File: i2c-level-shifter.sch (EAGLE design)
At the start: 11 parts, among them IC1 LP298XS, Q1 MMBF170, Q2 MMBF170

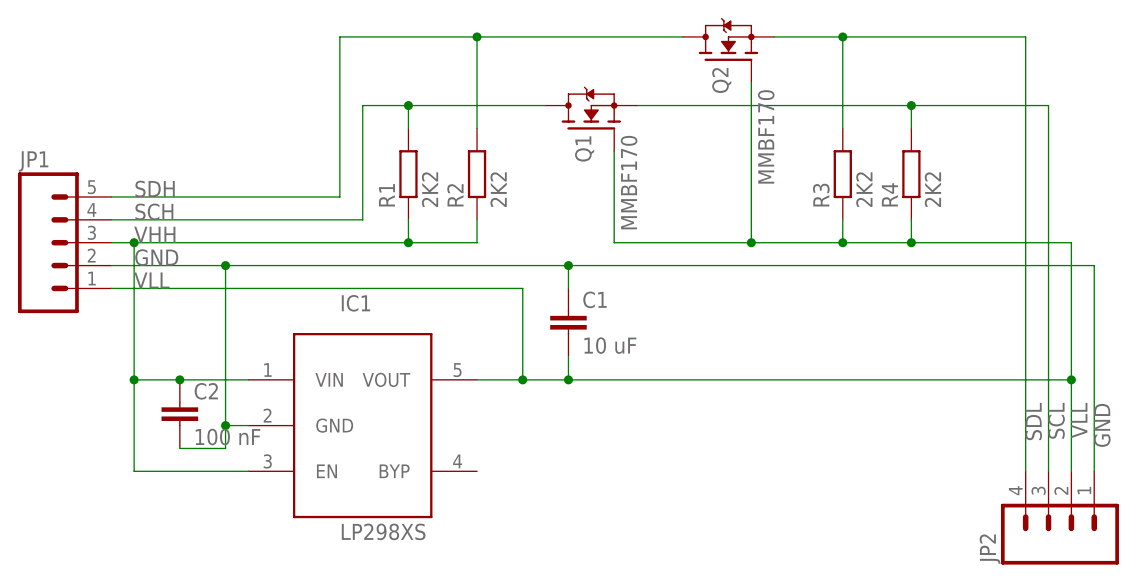
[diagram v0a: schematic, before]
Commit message: reversed headers
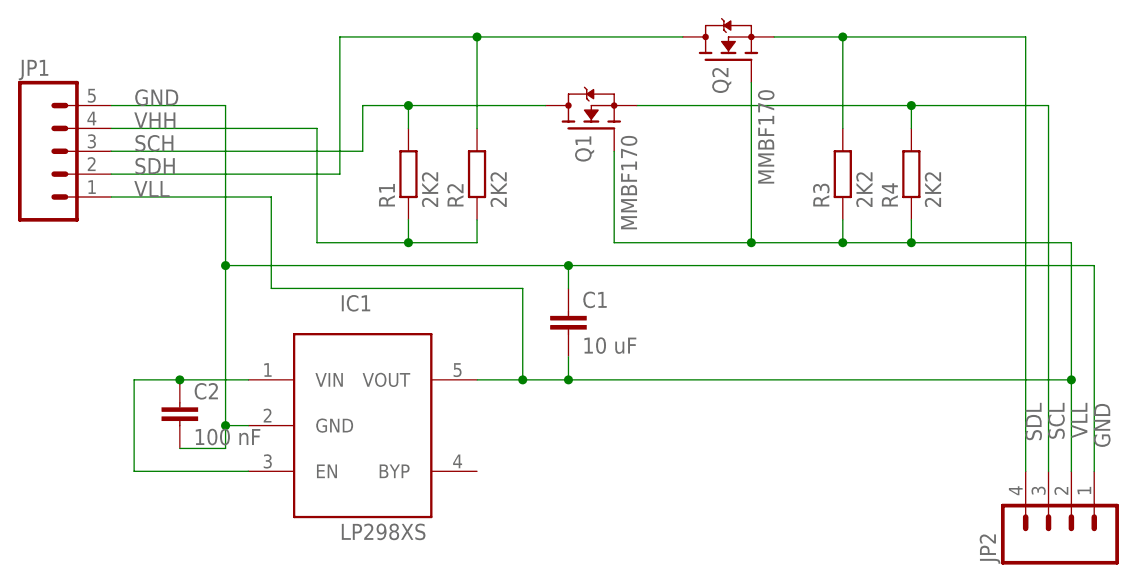
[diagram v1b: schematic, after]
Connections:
- net GND: now also JP1.5; no longer JP1.2
- net SCH: now also JP1.3; no longer JP1.4
- net SDH: now also JP1.2; no longer JP1.5
- net VHH: now also JP1.4; no longer JP1.3
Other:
- moved on the sheet: JP1
